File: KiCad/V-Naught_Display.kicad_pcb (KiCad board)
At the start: 2 copper layers, 70 x 35 mm, 24 parts, among them J1 USB_B_Micro, J2 I2C Header, J3 Conn_01x03, J4 Conn_01x02, SW1 SW_SPST, SW2 SW_SPST, SW3 SW_SPST, SW4 SW_SPST, SW5 SW_SPST, U1 AP2127K-3.3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

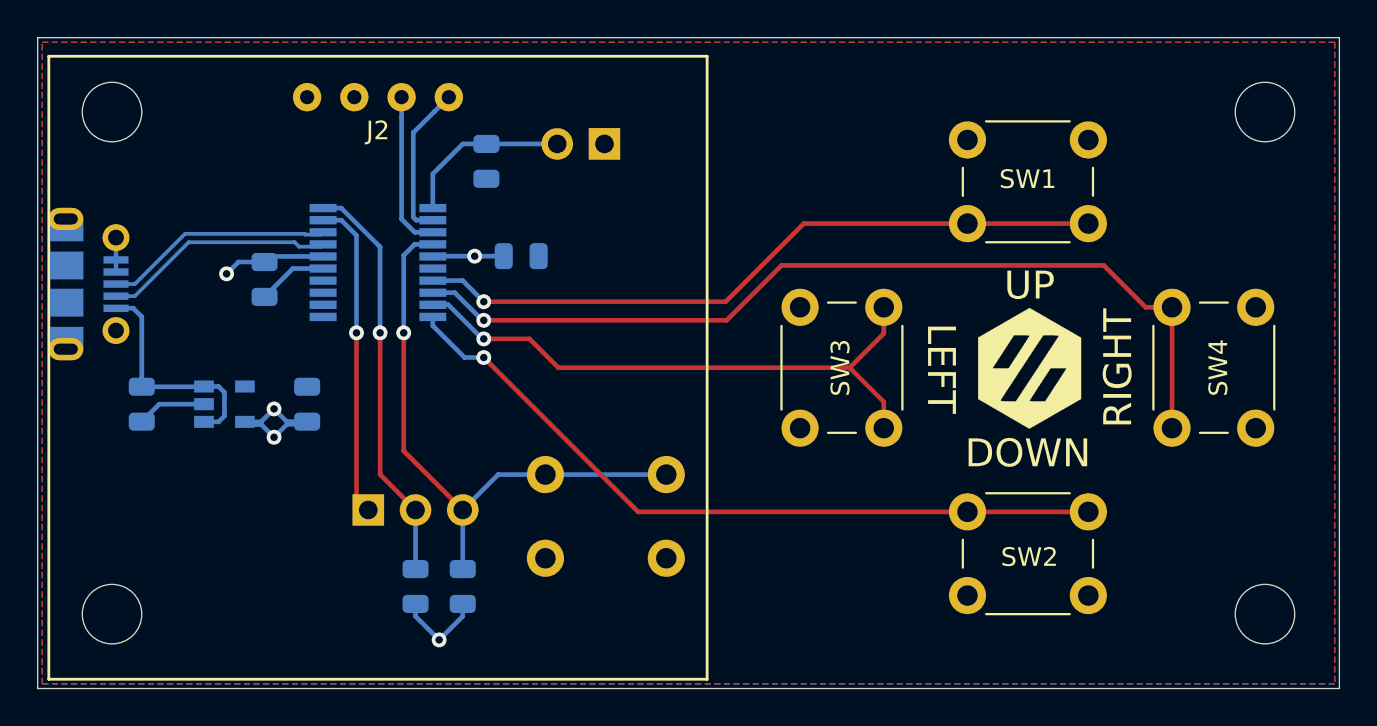
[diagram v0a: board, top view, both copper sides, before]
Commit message: Production File updates
Added a click encoder to the center of the buttons as an additional option for input instead of discrete buttons.

Klipper Config will follow with pinmaps when the boards arrive.
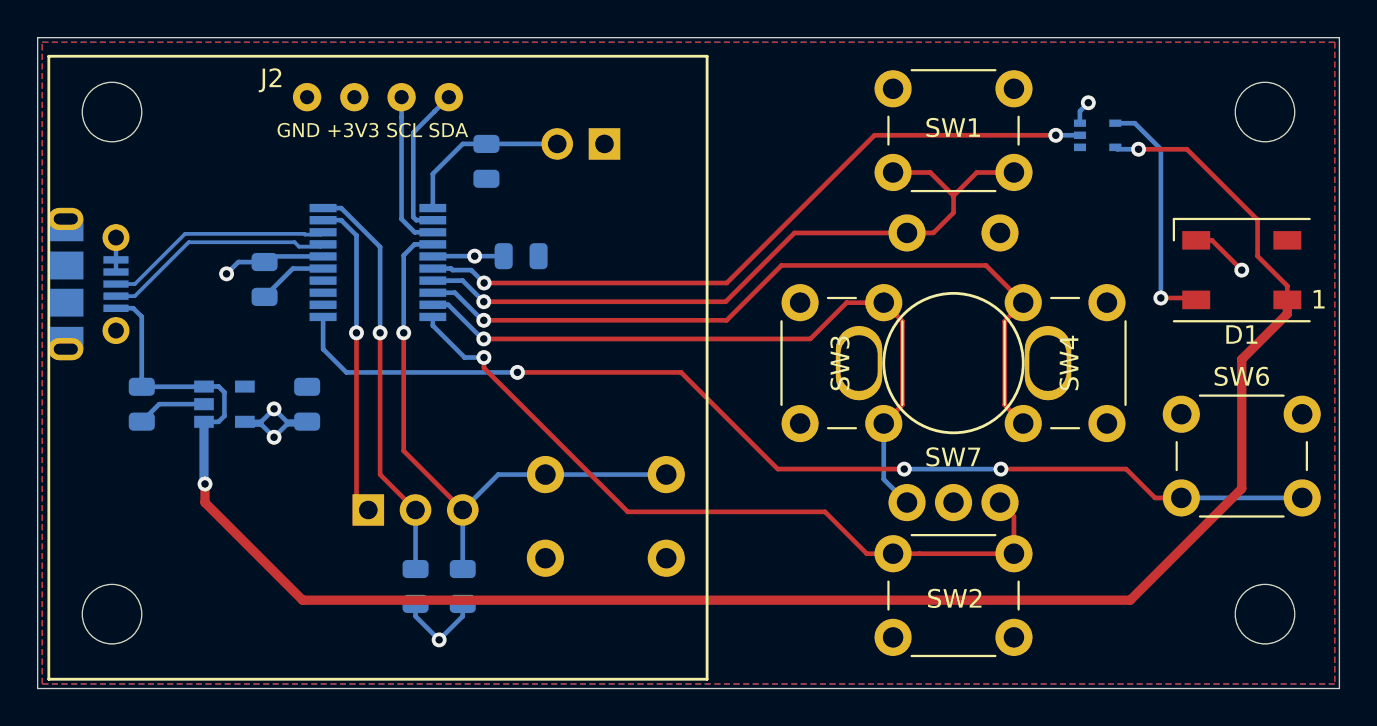
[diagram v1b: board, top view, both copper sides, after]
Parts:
- removed G*** (x2): LOGO, TRA_KiCad_Footprints:VoronLogo_6pt5mm_silkScreen
- added D1: WS2812B, LED_SMD:LED_WS2812B_PLCC4_5.0x5.0mm_P3.2mm, F.Cu at (159.9, 62.1)
- added SW6: SW_SPST, Button_Switch_THT:SW_PUSH_6mm, F.Cu at (156.7, 69.9)
- added SW7: Rotary_Encoder_Switch, TRA_KiCad_Footprints:EN11 Encoder, F.Cu at (144.4, 67.2)
- added U3: 74LVC1G17, Package_TO_SOT_SMD:SOT-353_SC-70-5, B.Cu at (152.2, 54.9)
- moved SW4 8.00 mm to (148.2, 70.4)
- moved SW1 4.85 mm to (147.7, 56.9)
- moved SW2 4.59 mm to (141.2, 77.4)
- moved SW3 0.25 mm to (140.7, 63.9)
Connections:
- U2 pad 11: (no net) -> Kill_Switch
- U2 pad 6: (no net) -> NeoPixel
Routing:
- net VBUS: track 12.4 -> 102.6 mm, vias 0 -> 2
- net Kill_Switch: track 0.00 -> 57.7 mm, vias 0 -> 3
- net NeoPixel: track 0.00 -> 38.4 mm, vias 0 -> 2
- net Net-(D1-Pad4): track 0.00 -> 13.0 mm, vias 0 -> 1
- net Button_Right: track 49.0 -> 41.7 mm
- net Button_Left: track 31.8 -> 38.6 mm
- net GND: track 9.37 -> 13.8 mm, vias 0 -> 2
- net Button_Up: track 37.5 -> 38.9 mm
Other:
- board text added: "GND +3V3 SCL SDA"
- board text added: "SDA SCL +3V3 GND"
- board text removed: "DOWN"
- board text removed: "LEFT"
- board text removed: "RIGHT"
- board text removed: "UP"

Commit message: Second I2C Header
Added a second I2C header for baords with reversed Vcc and Gnd pins.
Also added a full SWD header as well

Updated Production files
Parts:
- added J5: SWD Header, Connector_PinHeader_1.27mm:PinHeader_2x05_P1.27mm_Vertical_SMD, B.Cu at (107.6, 78.9)
- added J6: I2C Header 2, Connector_PinHeader_2.54mm:PinHeader_1x04_P2.54mm_Vertical, F.Cu at (109.7, 55.4)
- J2: value I2C Header -> I2C Header 1
- moved R2 5.52 mm to (124.4, 58.4), turned to 0 degrees
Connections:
- net Reset renamed ~Reset
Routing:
- net ~Reset: track 31.7 -> 47.5 mm, vias 1 -> 2
- net SWDCLK: track 22.0 -> 30.6 mm
- net SWDIO: track 17.2 -> 21.6 mm
- net GND: track 13.8 -> 18.0 mm
- net +3V3: track 22.2 -> 23.8 mm, vias 5 -> 6
- net BOOT0: track 9.20 -> 10.4 mm
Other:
- board text added: "+3V3 GND SCL SDA"
- board text added: "1 9"
- board text added: "2 10"
- board text added: "SDA SCL GND +3V3"
